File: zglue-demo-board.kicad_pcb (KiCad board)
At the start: 6 copper layers, 56 x 66 mm, 124 parts, among them J1 20021121-00010C4LF, J10 0473460001, J2 DF13A-2P-1.25H, J3 20021121-00010C4LF, J4 2x20_Header_Female, J5 0473460001, J6 556500488, J7 556500488, J8 WE_686115148922, J9 WE_686115148922_FLIPPED, U1 MCP1700T-3302E_TT, U2 NTB0104BQ, U3 NTB0104BQ, U4 NTB0104BQ, U5 93LC56CT-IMC, U6 FT4232HQ, Y1 ASFLMB-12.000MHZ-LC-T

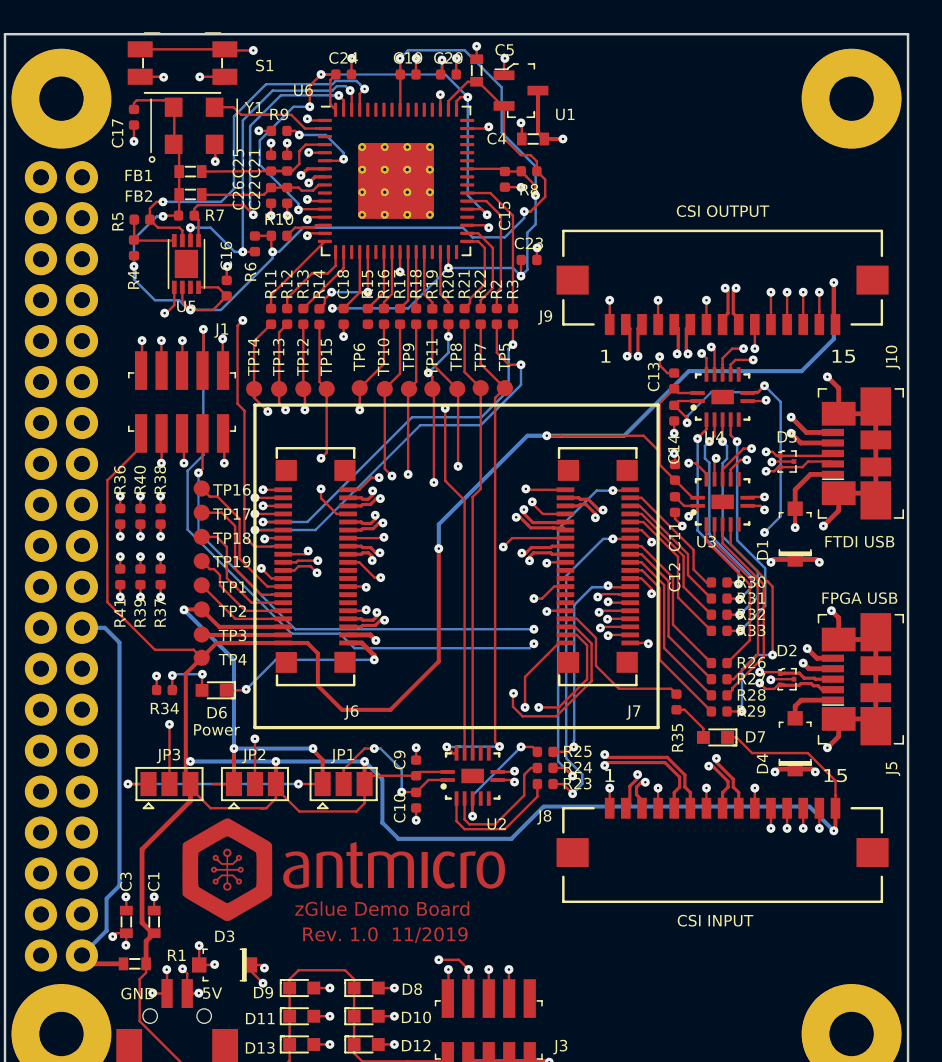
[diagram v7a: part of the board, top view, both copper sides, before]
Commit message: Added connections for I2C and UART
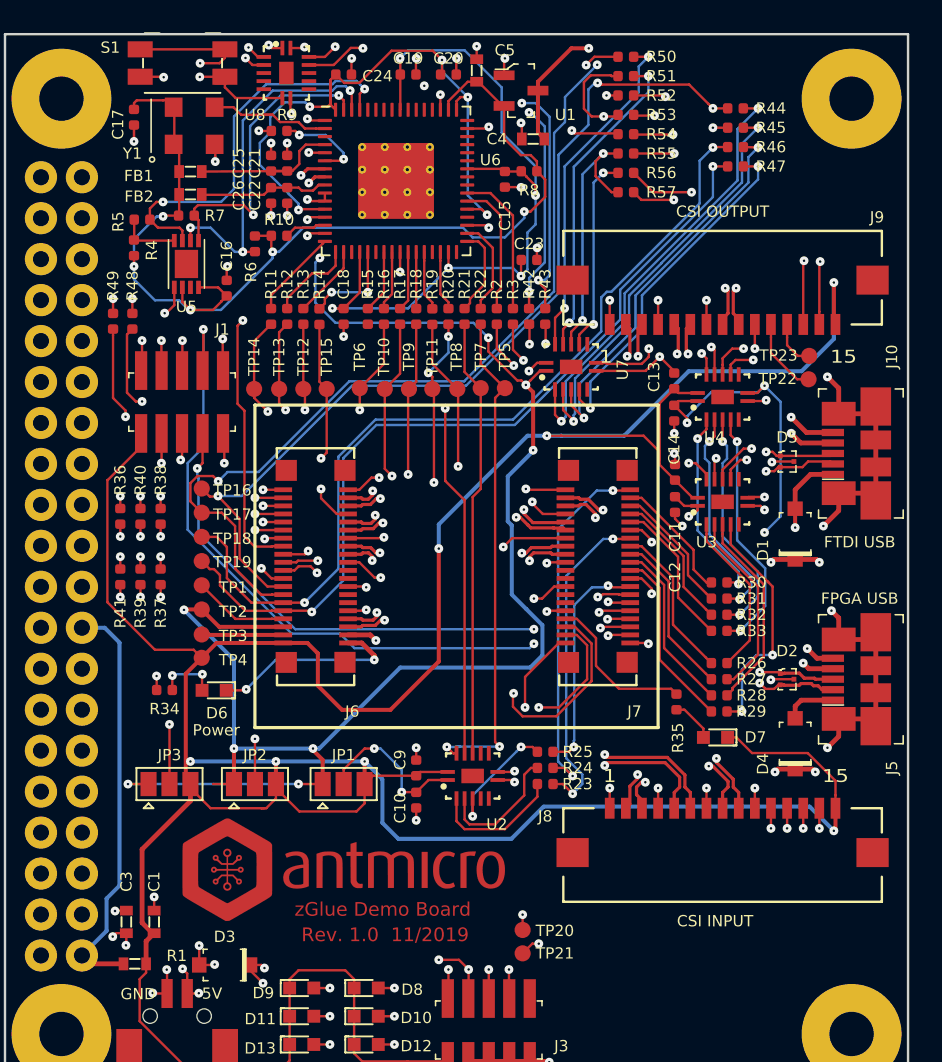
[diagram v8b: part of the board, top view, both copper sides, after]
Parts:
- added R42: R_0R_0402, antmicro-footprints:0402-res, F.Cu at (32.5, 17.5)
- added R43: R_0R_0402, antmicro-footprints:0402-res, F.Cu at (33.5, 17.5)
- added R44: R_0R_0402, antmicro-footprints:0402-res, F.Cu at (45.3, 4.60)
- added R45: R_0R_0402, antmicro-footprints:0402-res, F.Cu at (45.3, 5.80)
- added R46: R_0R_0402, antmicro-footprints:0402-res, F.Cu at (45.3, 7.00)
- added R47: R_0R_0402, antmicro-footprints:0402-res, F.Cu at (45.3, 8.20)
- added R48: R_0R_0402, antmicro-footprints:0402-res, F.Cu at (7.90, 17.8)
- added R49: R_0R_0402, antmicro-footprints:0402-res, F.Cu at (6.70, 17.8)
- added R50: R_0R_0402, antmicro-footprints:0402-res, F.Cu at (38.5, 1.40)
- added R51: R_0R_0402, antmicro-footprints:0402-res, F.Cu at (38.5, 2.60)
- added R52: R_0R_0402, antmicro-footprints:0402-res, F.Cu at (38.5, 3.80)
- added R53: R_0R_0402, antmicro-footprints:0402-res, F.Cu at (38.5, 5.00)
- added R54: R_0R_0402, antmicro-footprints:0402-res, F.Cu at (38.5, 6.20)
- added R55: R_0R_0402, antmicro-footprints:0402-res, F.Cu at (38.5, 7.40)
- added R56: R_0R_0402, antmicro-footprints:0402-res, F.Cu at (38.5, 8.60)
- added R57: R_0R_0402, antmicro-footprints:0402-res, F.Cu at (38.5, 9.80)
- added TP20: TP_SMD1MM, antmicro-footprints:Testpoint_smd_1mm, F.Cu at (32.1, 55.6)
- added TP21: TP_SMD1MM, antmicro-footprints:Testpoint_smd_1mm, F.Cu at (32.1, 57.1)
- added TP22: TP_SMD1MM, antmicro-footprints:Testpoint_smd_1mm, F.Cu at (49.8, 21.5)
- added TP23: TP_SMD1MM, antmicro-footprints:Testpoint_smd_1mm, F.Cu at (49.9, 20.0)
- added U7: NTB0104BQ, antmicro-footprints:QDHVQFN14, F.Cu at (35.1, 20.6)
- added U8: NTB0104BQ, antmicro-footprints:QDHVQFN14, F.Cu at (17.4, 2.41)
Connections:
- C3 pad 1: /5V0_IN -> GND
- C3 pad 2: GND -> /5V0_IN
- J4 pad 3: Net-(J4-Pad3) -> /RPI_SDA
- J4 pad 5: Net-(J4-Pad5) -> /RPI_SCL
- J8 pad 11: /CAM_GPIO -> /CAM_GPIO_IN
- J8 pad 12: /CAM_CLK -> /CAM_CLK_IN
- J8 pad 13: /CAM_SCL -> /CAM_SCL_IN
- J8 pad 14: /CAM_SDA -> /CAM_SDA_IN
- J9 pad 11: /CAM_GPIO -> /CAM_GPIO_OUT
- J9 pad 12: /CAM_CLK -> /CAM_CLK_OUT
- J9 pad 13: /CAM_SCL -> /CAM_SCL_OUT
- J9 pad 14: /CAM_SDA -> /CAM_SDA_OUT
- R2 pad 2: /DBG_RX -> /DBG_RX_3V3
- R3 pad 2: /DBG_TX -> /DBG_TX_3V3
- U6 pad 10: Net-(U6-Pad10) -> GND
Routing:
- net /1V8_SYS: track 40.7 -> 125.4 mm, vias 5 -> 12
- net /RPI_SDA: track 0.00 -> 80.7 mm, vias 0 -> 2
- net /RPI_SCL: track 0.00 -> 76.3 mm, vias 0 -> 1
- net /CAM_SCL_IN: track 0.00 -> 60.3 mm, vias 0 -> 3
- net /CAM_SDA_IN: track 0.00 -> 59.9 mm, vias 0 -> 3
- net Net-(J4-Pad8): track 0.00 -> 59.4 mm, vias 0 -> 1
- net Net-(J4-Pad10): track 0.00 -> 58.9 mm, vias 0 -> 1
- net /I2C_0_SDA: track 8.70 -> 64.4 mm, vias 0 -> 3
- net /I2C_0_SCL: track 9.02 -> 58.4 mm, vias 0 -> 3
- net /3V3_SYS: track 236.6 -> 284.1 mm, vias 7 -> 10
- net /I2C_1_SCL: track 7.87 -> 54.0 mm, vias 0 -> 2
- net /I2C_1_SDA: track 6.71 -> 52.4 mm, vias 0 -> 2
- net /CAM_GPIO: track 40.8 -> 0.00 mm, vias 2 -> 0
- net /CAM_CLK: track 40.2 -> 0.00 mm, vias 2 -> 0
- net /CAM_SDA: track 39.9 -> 0.00 mm, vias 2 -> 0
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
